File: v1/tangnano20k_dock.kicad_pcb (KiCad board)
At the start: 2 copper layers, 160 x 57.2 mm, 50 parts, among them J1 Mini-DIN-6, J2 Conn_01x02, J3 DB15_Female_HighDensity, J4 DB9_Male, J5 Conn_02x16_Odd_Even, J6 FCR684205T, J7 RCA, J8 RCA, J9 RCA, U1 TXS0104E, U2 TangNano20K, U3 CS4354

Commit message: Everything connected
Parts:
- removed the J8 at (226.0, 142.0)
- added J6: Conn_02x10_Odd_Even, Connector_PinHeader_2.54mm:PinHeader_2x10_P2.54mm_Vertical, F.Cu at (142.9, 129.5)
- J3: value DB15_Female_HighDensity -> DB15_Female_HighDensity_MountingHoles; footprint Connector_Dsub:DSUB-15-HD_Female_Horizontal_P2.29x1.98mm_EdgePinOffset9.40mm -> Connector_Dsub:DSUB-15-HD_Female_Horizontal_P2.29x1.98mm_EdgePinOffset8.35mm_Housed_MountingHolesOffset10.89mm; moved to F.Cu
- J5: value Conn_02x16_Odd_Even -> Conn_02x10_Odd_Even; footprint Connector_PinHeader_2.54mm:PinHeader_2x16_P2.54mm_Vertical -> Connector_PinHeader_2.54mm:PinHeader_2x10_P2.54mm_Vertical
- J9: value RCA -> AudioJack3; footprint TangNano20k:phono -> Connector_Audio:Jack_3.5mm_Lumberg_1503_07_Horizontal
- moved J1 112.5 mm to (194.3, 95.2), turned to 0 degrees
- moved R1 103.3 mm to (184.8, 102.9), turned to 180 degrees
- moved R2 101.1 mm to (184.8, 99.7), turned to 180 degrees
- moved R3 98.5 mm to (184.8, 96.5), turned to 180 degrees
- moved R4 96.7 mm to (184.8, 93.3), turned to 180 degrees
- moved R16 82.5 mm to (163.2, 117.5), turned to 90 degrees
- moved JP1 81.1 mm to (174.6, 114.3)
- moved C1 72.2 mm to (166.4, 103.5)
- moved U1 72.1 mm to (160.7, 101.6), turned to 0 degrees
- moved C2 68.2 mm to (155.1, 102.9), turned to 90 degrees
- moved J2 62.5 mm to (143.5, 92.7), turned to -90 degrees
- moved RN1 54.0 mm to (184.8, 106.6)
- moved R18 49.9 mm to (155.6, 126.6), turned to 0 degrees
- moved J8 46.8 mm to (139.1, 137.4)
- moved R17 45.3 mm to (155.6, 132.7), turned to 0 degrees
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- renumbered J6 to J8
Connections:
- C10 pad 2: Net-(JP2-Pad2) -> Net-(C10-Pad2)
- J5 pad 1: Net-(J5-Pad1) -> GND
- J5 pad 10: /GPIO11 -> Net-(J5-Pad10)
- J5 pad 11: Net-(J5-Pad11) -> /GPIO12
- J5 pad 12: /GPIO10 -> Net-(J5-Pad12)
- J5 pad 13: Net-(J5-Pad13) -> /GPIO13
- J5 pad 14: /GPIO9 -> Net-(J5-Pad14)
- J5 pad 15: Net-(J5-Pad15) -> /GPIO14
- J5 pad 16: /GPIO8 -> Net-(J5-Pad16)
- J5 pad 17: Net-(J5-Pad17) -> /GPIO15
- J5 pad 18: /GPIO7 -> Net-(J5-Pad18)
- J5 pad 19: Net-(J5-Pad19) -> unconnected-(J5-Pad19)
- J5 pad 2: /GPIO15 -> GND
- J5 pad 20: /GPIO6 -> unconnected-(J5-Pad20)
- J5 pad 3: Net-(J5-Pad3) -> /GPIO8
- J5 pad 4: /GPIO14 -> Net-(J5-Pad4)
- J5 pad 5: Net-(J5-Pad5) -> /GPIO9
- J5 pad 6: /GPIO13 -> Net-(J5-Pad6)
- J5 pad 7: Net-(J5-Pad7) -> /GPIO10
- J5 pad 8: /GPIO12 -> Net-(J5-Pad8)
- J5 pad 9: Net-(J5-Pad9) -> /GPIO11
- JP2 pad 2: Net-(JP2-Pad2) -> Net-(C10-Pad2)
- RN1 pad 2: Net-(J5-Pad1) -> Net-(J5-Pad4)
- RN1 pad 3: Net-(J5-Pad3) -> Net-(J5-Pad6)
- RN1 pad 4: Net-(J5-Pad5) -> Net-(J5-Pad8)
- RN1 pad 5: Net-(J5-Pad7) -> Net-(J5-Pad10)
- RN1 pad 6: Net-(J5-Pad9) -> Net-(J5-Pad12)
- RN1 pad 7: Net-(J5-Pad11) -> Net-(J5-Pad14)
- RN1 pad 8: Net-(J5-Pad13) -> Net-(J5-Pad16)
- RN1 pad 9: Net-(J5-Pad15) -> Net-(J5-Pad18)
- RN2 pad 2: Net-(J5-Pad31) -> Net-(RN2-Pad2)
- RN2 pad 3: Net-(J5-Pad29) -> Net-(RN2-Pad3)
- RN2 pad 4: Net-(J5-Pad27) -> Net-(RN2-Pad4)
- RN2 pad 5: Net-(J5-Pad25) -> Net-(RN2-Pad5)
- RN2 pad 6: Net-(J5-Pad23) -> Net-(J6-Pad12)
- RN2 pad 7: Net-(J5-Pad21) -> Net-(J6-Pad14)
- RN2 pad 8: Net-(J5-Pad19) -> Net-(RN2-Pad8)
- RN2 pad 9: Net-(J5-Pad17) -> Net-(RN2-Pad9)
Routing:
- net +3.3V: track 40.8 -> 193.9 mm
- net +5V: track 0.00 -> 82.0 mm
- net /JS_FIRE2: track 0.00 -> 53.9 mm
- net /JS_FIRE1: track 0.00 -> 47.2 mm
- net /GPIO12: track 73.9 -> 31.9 mm
- net /GPIO10: track 47.8 -> 8.70 mm
- net /I2S_LRCLK: track 0.00 -> 37.4 mm
- net /I2S_MCLK: track 0.00 -> 36.8 mm
- net /GPIO13: track 80.0 -> 45.7 mm
- net /JS_RIGHT: track 47.0 -> 78.9 mm
- net /I2S_SDIN: track 0.00 -> 28.9 mm
- net /GPIO9: track 37.3 -> 9.70 mm
- net /JS_DOWN: track 58.4 -> 84.4 mm
- net /I2S_SCLK: track 0.00 -> 24.7 mm
- net /SPDIF: track 11.5 -> 33.0 mm
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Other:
- board size 160 x 57.2 mm -> 114.9 x 57.2 mm

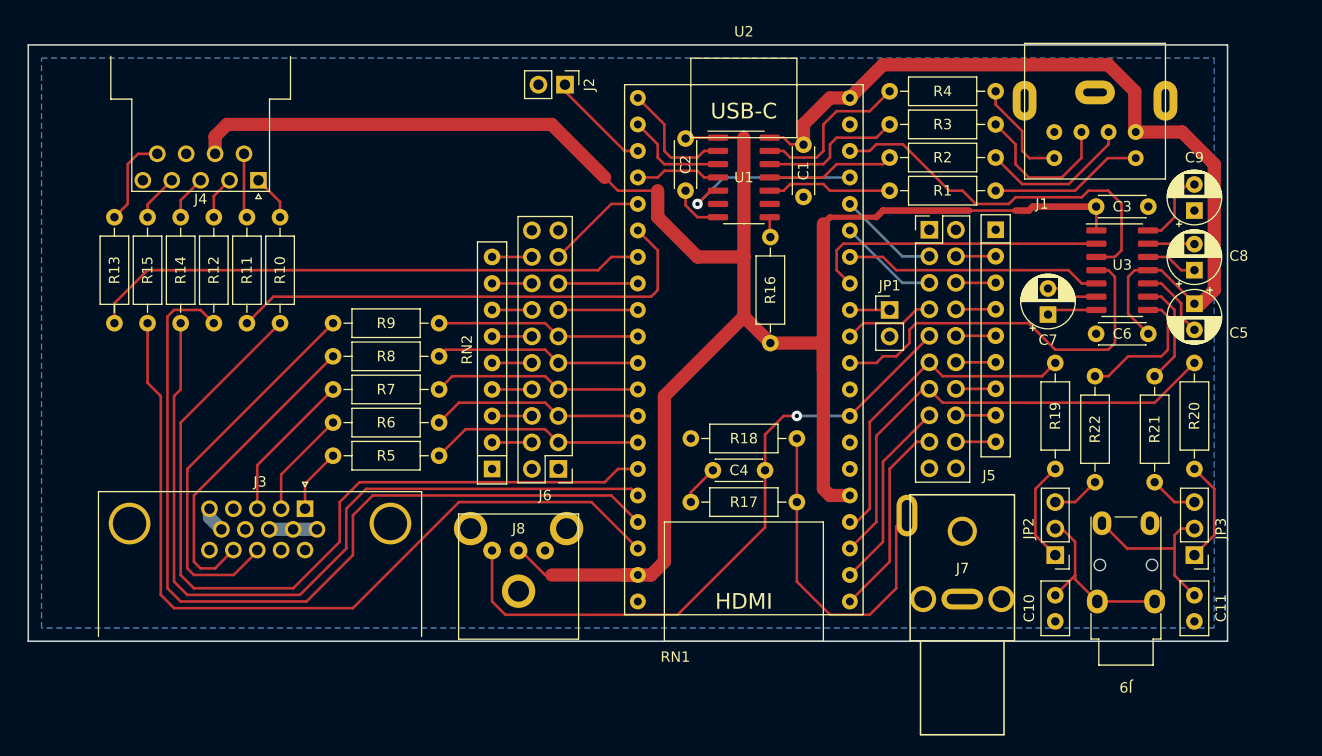
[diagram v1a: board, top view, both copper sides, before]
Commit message: Much tidying up, corrected VGA footprint
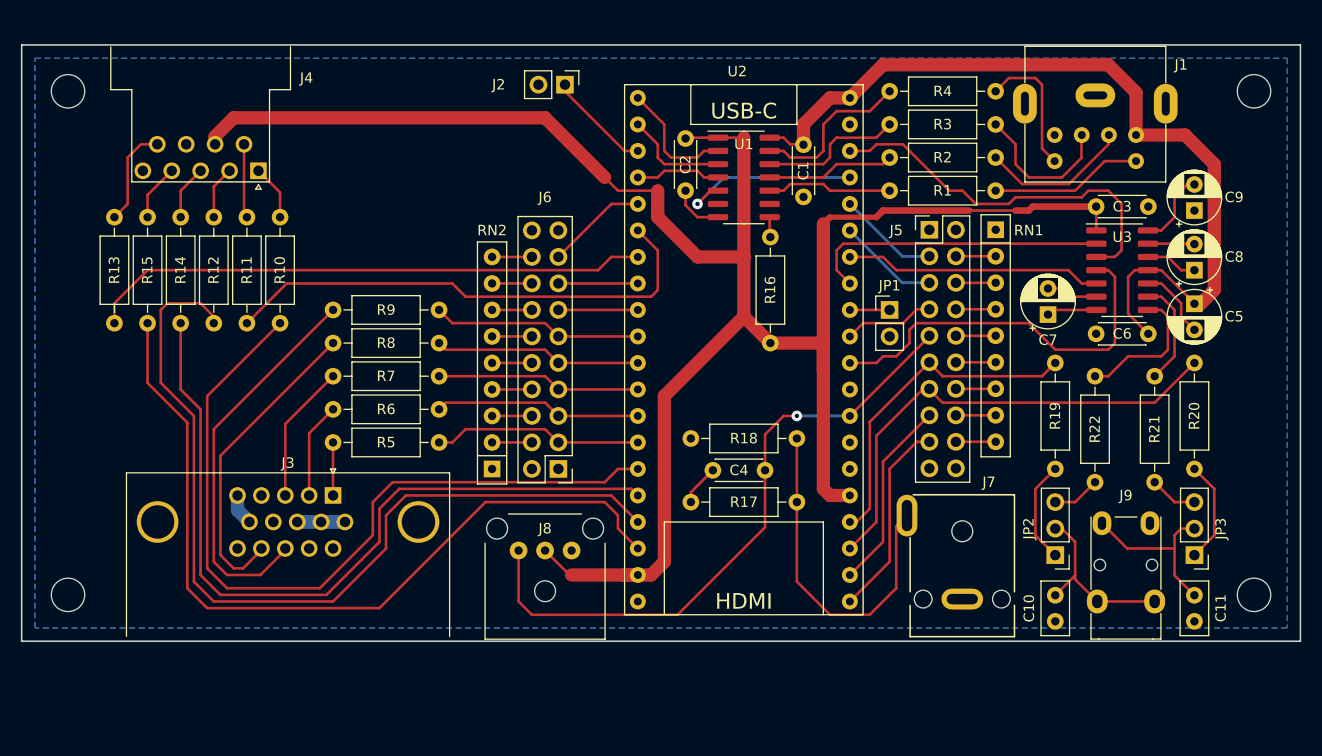
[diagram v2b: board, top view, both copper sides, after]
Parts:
- added H1: MountingHole, MountingHole:MountingHole_3.2mm_M3, F.Cu at (95.9, 93.3)
- added H2: MountingHole, MountingHole:MountingHole_3.2mm_M3, F.Cu at (209.6, 93.3)
- added H3: MountingHole, MountingHole:MountingHole_3.2mm_M3, F.Cu at (95.9, 141.6)
- added H4: MountingHole, MountingHole:MountingHole_3.2mm_M3, F.Cu at (209.6, 141.6)
- J3: footprint Connector_Dsub:DSUB-15-HD_Female_Horizontal_P2.29x1.98mm_EdgePinOffset8.35mm_Housed_MountingHolesOffset10.89mm -> TangNano20k:DSUB-15-HD_Female_Horizontal_P2.29x1.98mm_EdgePinOffset8.35mm_Housed_MountingHolesOffset10.89mm
- J9: footprint Connector_Audio:Jack_3.5mm_Lumberg_1503_07_Horizontal -> TangNano20k:Jack_3.5mm_Lumberg_1503_07_Horizontal
- R10, R11, R12, R13, R14, R15: value 390 -> 180
- moved J3 2.97 mm to (121.3, 132.1)
- moved J8 2.54 mm to (141.6, 137.4)
- moved J1 2.29 mm to (194.3, 97.5)
- moved R5 1.27 mm to (121.3, 127.0)
- moved R8 1.27 mm to (121.3, 117.5)
- moved R6 1.27 mm to (121.3, 123.8)
- moved R7 1.27 mm to (121.3, 120.7)
- moved R9 1.27 mm to (121.3, 114.3)
- moved J4 0.91 mm to (114.1, 101.0)
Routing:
- net /JS_UP: track 79.4 -> 75.0 mm
- net Net-(J1-Pad5): track 10.1 -> 13.0 mm
- net /JS_LEFT: track 76.7 -> 73.9 mm
- net +3.3V: track 193.9 -> 191.2 mm
- net /GPIO11: track 63.6 -> 61.0 mm
- net /JS_RIGHT: track 78.9 -> 77.7 mm
- net /VGA_G: track 10.3 -> 9.20 mm
- net /VGA_B: track 14.4 -> 13.3 mm
- net /VGA_R: track 6.19 -> 5.08 mm
- net /JS_FIRE1: track 47.2 -> 48.2 mm
- net /JS_6: track 5.79 -> 6.70 mm
- net /JS_4: track 4.50 -> 5.41 mm
- net /JS_3: track 4.33 -> 5.24 mm
- net /JS_2: track 4.16 -> 5.07 mm
- net /JS_1: track 4.39 -> 5.30 mm
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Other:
- board size 114.9 x 57.2 mm -> 122.6 x 57.2 mm

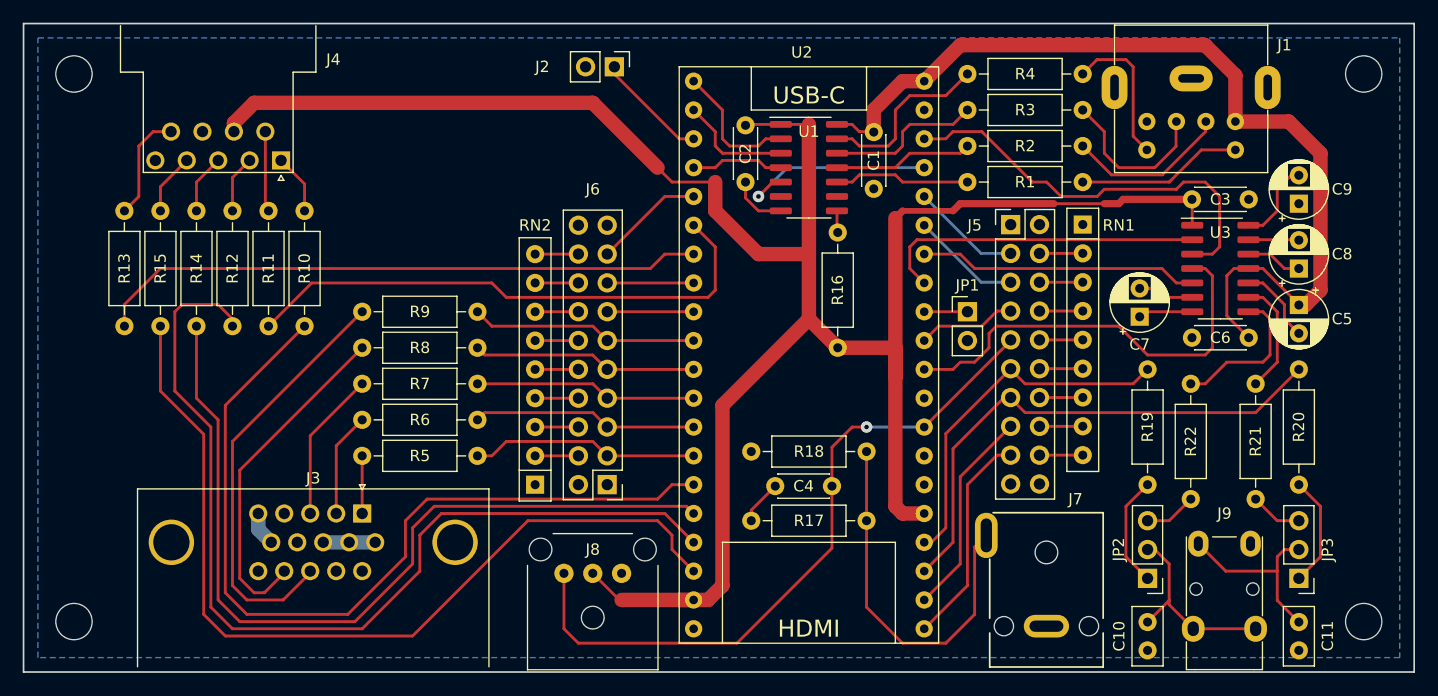
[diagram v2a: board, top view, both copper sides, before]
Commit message: Corrected Joystick footprint
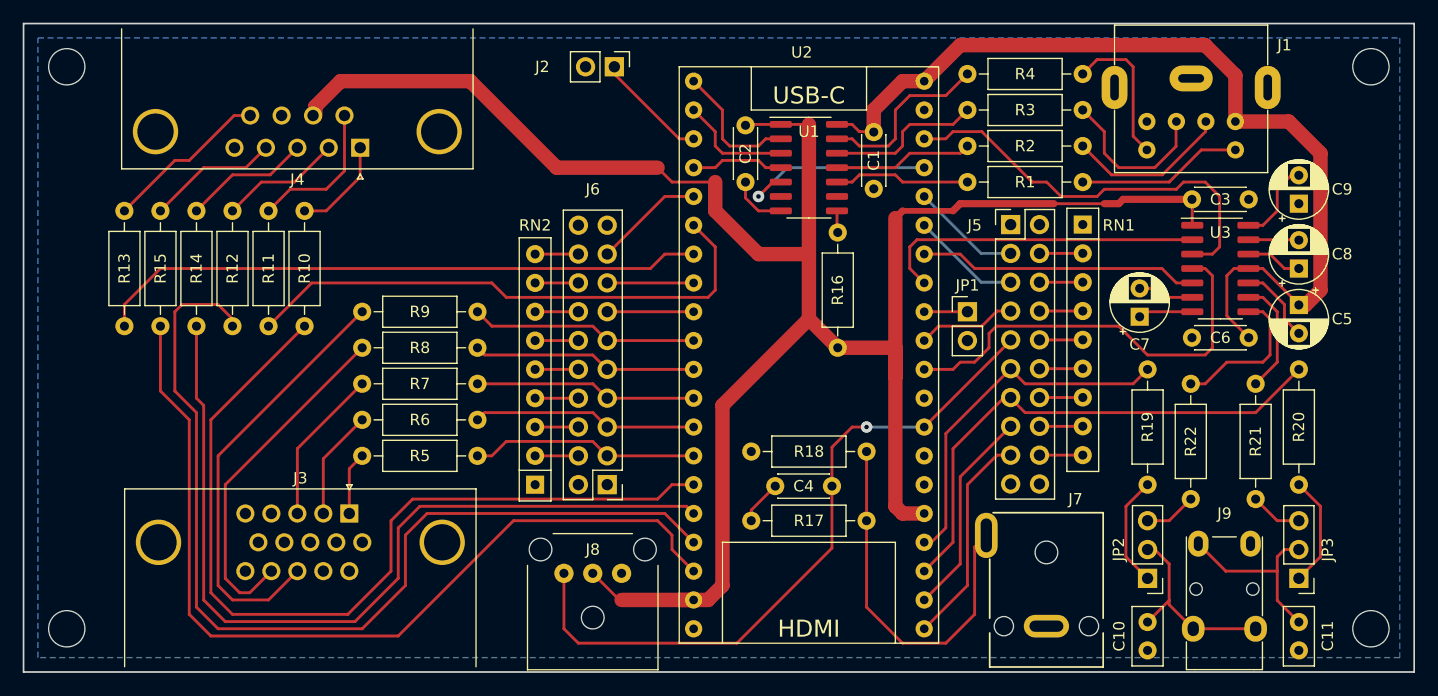
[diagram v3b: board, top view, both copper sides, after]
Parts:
- J4: value DB9_Male -> DB9_Male_MountingHoles; footprint Connector_Dsub:DSUB-9_Male_Horizontal_P2.77x2.54mm_EdgePinOffset9.40mm -> Connector_Dsub:DSUB-9_Male_Horizontal_P2.77x2.84mm_EdgePinOffset7.70mm_Housed_MountingHolesOffset9.12mm
- moved J4 7.06 mm to (121.1, 99.8)
- moved J3 1.13 mm to (120.2, 132.1)
- moved H3 0.90 mm to (95.2, 142.2)
- moved H1 0.90 mm to (95.2, 92.7)
- moved H4 0.90 mm to (210.2, 142.2)
- moved H2 0.90 mm to (210.2, 92.7)
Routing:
- net GND: track 24.6 -> 17.0 mm
- net /JS_6: track 6.70 -> 13.0 mm
- net /JS_4: track 5.41 -> 11.6 mm
- net +3.3V: track 191.2 -> 185.0 mm
- net /JS_3: track 5.24 -> 11.2 mm
- net /JS_2: track 5.07 -> 10.8 mm
- net /JS_9: track 9.61 -> 14.6 mm
- net /JS_1: track 5.30 -> 8.71 mm
- net /JS_UP: track 75.0 -> 77.6 mm
- net /JS_LEFT: track 73.9 -> 75.4 mm
- net /JS_DOWN: track 83.7 -> 85.2 mm
- net /JS_RIGHT: track 77.7 -> 78.5 mm
- net /VGA_HS: track 37.2 -> 38.0 mm
- net /VGA_VS: track 30.0 -> 30.7 mm

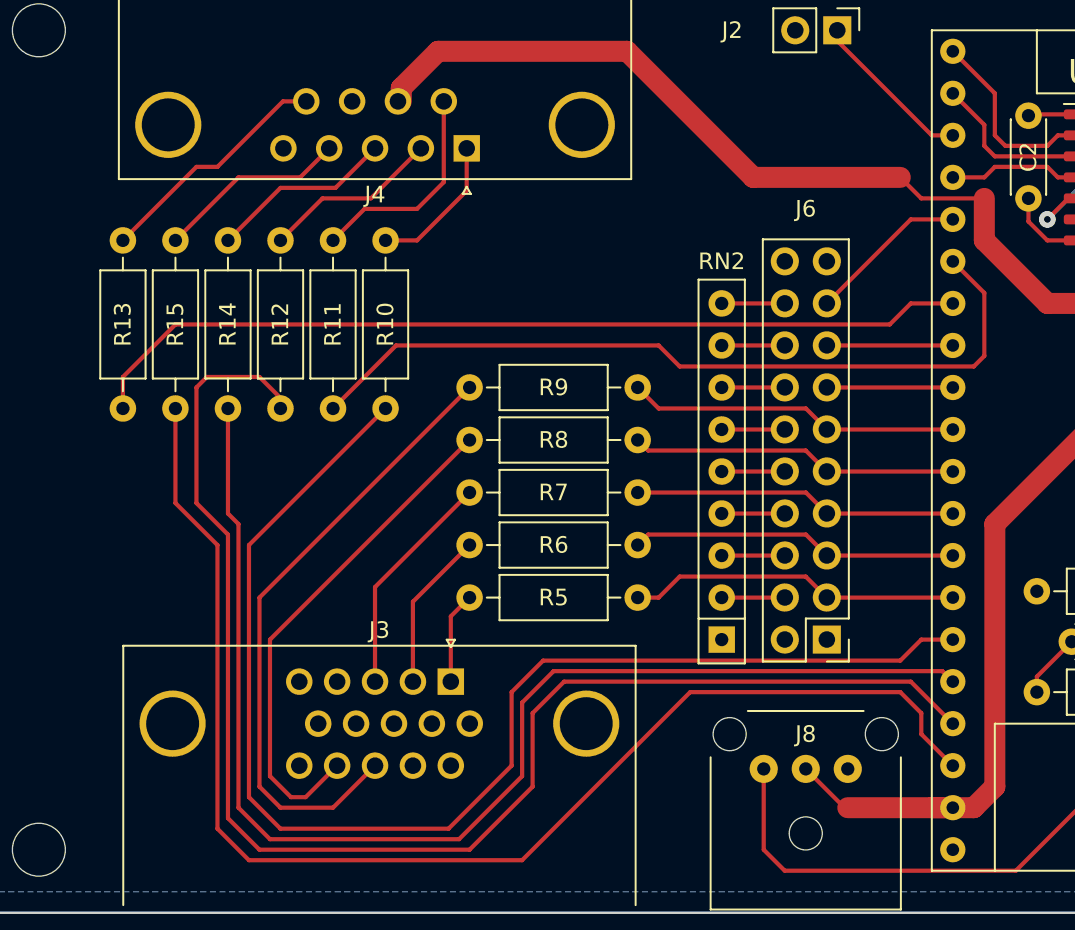
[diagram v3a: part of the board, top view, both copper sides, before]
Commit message: Re-orient resistors
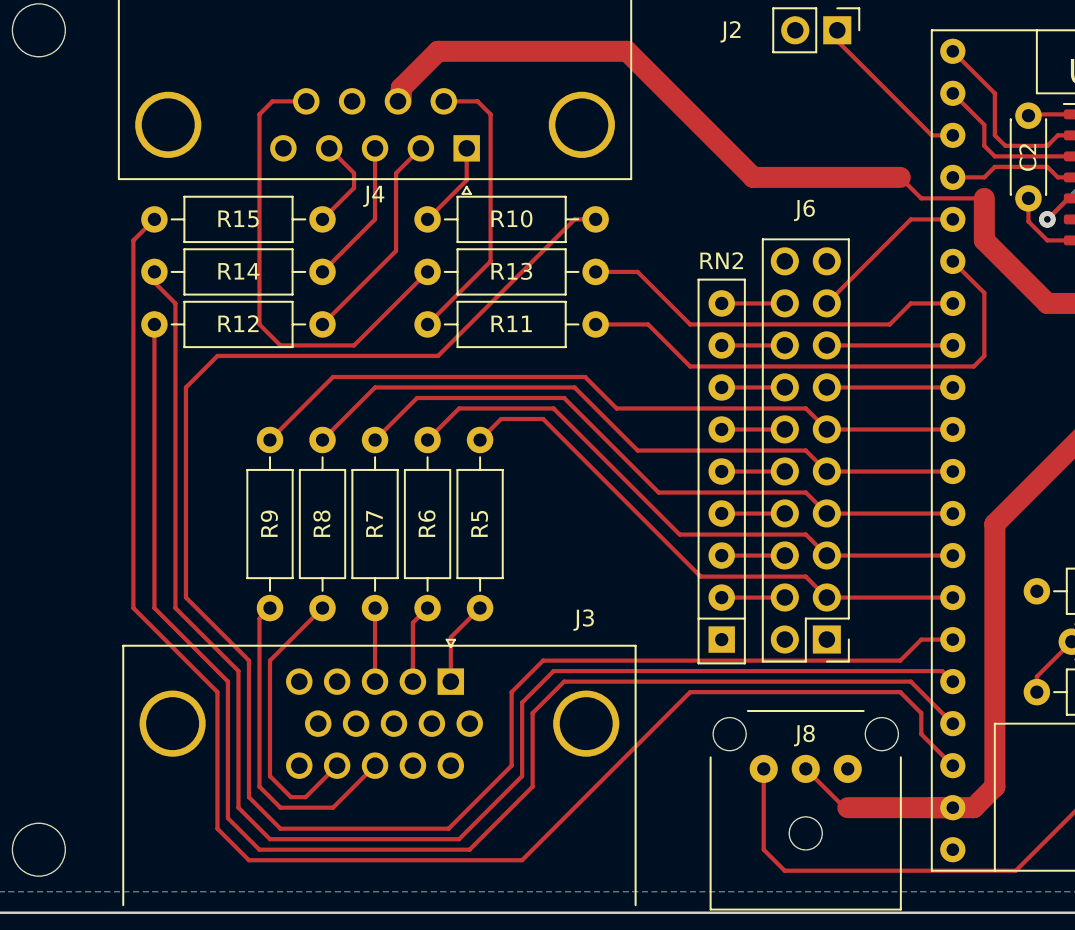
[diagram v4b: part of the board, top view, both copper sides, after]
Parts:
- moved R13 18.5 mm to (118.7, 107.3), turned to 0 degrees
- moved R9 18.0 mm to (109.2, 127.6), turned to 90 degrees
- moved R8 13.5 mm to (112.4, 127.6), turned to 90 degrees
- moved R7 9.03 mm to (115.6, 127.6), turned to 90 degrees
- moved R15 8.98 mm to (112.4, 104.1), turned to 180 degrees
- moved R11 7.65 mm to (118.7, 110.5), turned to 0 degrees
- moved R14 6.02 mm to (112.4, 107.3), turned to 180 degrees
- moved R12 5.68 mm to (112.4, 110.5), turned to 180 degrees
- moved R6 4.58 mm to (118.7, 127.6), turned to 90 degrees
- moved R10 2.84 mm to (118.7, 104.1), turned to 0 degrees
- moved R5 0.90 mm to (121.9, 127.6), turned to 90 degrees
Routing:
- net /JS_FIRE2: track 53.9 -> 23.4 mm
- net /JS_UP: track 77.6 -> 106.0 mm
- net /GPIO4: track 20.1 -> 44.2 mm
- net /GPIO3: track 19.8 -> 41.5 mm
- net /GPIO2: track 19.6 -> 38.9 mm
- net /VGA_HS: track 38.0 -> 19.6 mm
- net /JS_FIRE1: track 48.2 -> 31.3 mm
- net /GPIO1: track 19.8 -> 36.2 mm
- net /VGA_VS: track 30.7 -> 16.9 mm
- net /JS_9: track 14.6 -> 28.4 mm
- net /GPIO0: track 20.1 -> 33.6 mm
- net /JS_RIGHT: track 78.5 -> 91.5 mm
- net /JS_LEFT: track 75.4 -> 84.9 mm
- net /VGA_B: track 13.8 -> 4.45 mm
- net /JS_4: track 11.6 -> 5.71 mm
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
